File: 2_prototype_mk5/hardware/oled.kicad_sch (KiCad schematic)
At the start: 1 part, among them J6 Conn_01x04_Pin

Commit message: MKV revision 1
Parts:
- J6: LCSC Part Number (none) -> C124378; LCSC_Part_Number C124378 -> (none)
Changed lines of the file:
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@@
 			)
 		)
-		(property "LCSC_Part_Number" "C124378"
+		(property "LCSC Part Number" "C124378"
 			(at 128.27 93.98 0)
 			(hide yes)

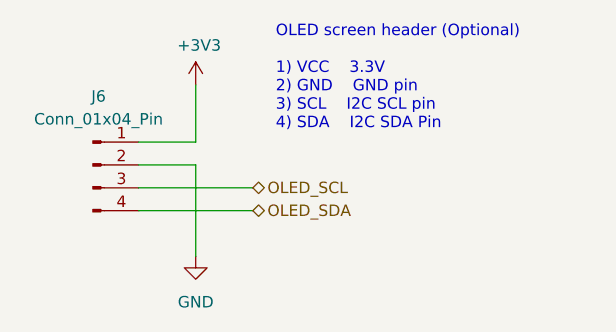
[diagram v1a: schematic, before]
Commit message: Cost reductions for JCLPCB
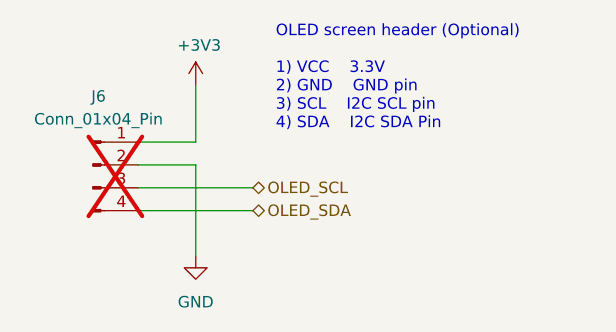
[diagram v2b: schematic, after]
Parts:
- J6: now not fitted; now left out of the parts list
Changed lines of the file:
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@@
 		(body_style 1)
 		(exclude_from_sim no)
-		(in_bom yes)
+		(in_bom no)
 		(on_board yes)
 		(in_pos_files yes)
-		(dnp no)
+		(dnp yes)
 		(fields_autoplaced yes)
 		(property "Reference" "J6"
